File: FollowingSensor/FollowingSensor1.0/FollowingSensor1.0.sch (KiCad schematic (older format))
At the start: 31 parts, among them J1 Conn_01x18, Q1 TEMT7100X01, Q10 TEMT7100X01, Q11 TEMT7100X01, Q12 TEMT7100X01, Q13 TEMT7100X01, Q14 TEMT7100X01, Q2 TEMT7100X01, Q3 TEMT7100X01, Q4 TEMT7100X01, Q5 TEMT7100X01, Q6 TEMT7100X01, Q7 TEMT7100X01, Q8 TEMT7100X01, Q9 TEMT7100X01

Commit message: LinesensorUpdate
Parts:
- D1, D2, D3, D4, D5, D6, D7, D8: symbol Device:LED_ALT -> FollowingSensor1.0-rescue:LED_ALT-Device
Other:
- moved on the sheet: D1, D2, D3, D4, D5, D6, D7, D8, J1, Q1, Q10, Q11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

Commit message: placement phototransister
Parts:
- added D11, D2, D4, D9: SIR19-21C/TR8, Footprint:SIR19-21C, symbol FollowingSensor1.0-rescue:LED_ALT-Device
- added R10, R11, R12, R9: R, Resistor_SMD:R_0603_1608Metric, symbol Device:R
- renumbered D7 to D10, D8 to D12, D2 to D3, D3 to D5, D4 to D6, D5 to D7, D6 to D8, Q14 to Q13, Q13 to Q14
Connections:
- net +3V3: now also R10.1, R11.1, R12.1, R9.1
- net SENSOR_PULSE: now also D11.1 (K), D2.1 (K), D4.1 (K), D9.1 (K)
- new net: D9.2 (A), R10.2
- new net: D11.2 (A), R12.2
- new net: D4.2 (A), R11.2
- new net: D2.2 (A), R9.2
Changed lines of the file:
@@
 $EndComp
 $Comp
-L FollowingSensor1.0-rescue:LED_ALT-Device D5
+L FollowingSensor1.0-rescue:LED_ALT-Device D7
 U 1 1 5F240BF8
 P 8950 2650
-F 0 "D5" V 8989 2532 50  0000 R CNN
+F 0 "D7" V 8989 2532 50  0000 R CNN
 F 1 "SIR19-21C/TR8" V 9100 2600 50  0000 R CNN
 F 2 "Footprint:SIR19-21C" H 8950 2650 50  0001 C CNN
@@
 $EndComp
 $Comp
-L FollowingSensor1.0-rescue:LED_ALT-Device D4
+L FollowingSensor1.0-rescue:LED_ALT-Device D6
 U 1 1 5F2485DD
 P 6950 2600
-F 0 "D4" V 6989 2482 50  0000 R CNN
+F 0 "D6" V 6989 2482 50  0000 R CNN
 F 1 "SIR19-21C/TR8" V 7100 2600 50  0000 R CNN
 F 2 "Footprint:SIR19-21C" H 6950 2600 50  0001 C CNN
@@
 $EndComp
 $Comp
-L FollowingSensor1.0-rescue:LED_ALT-Device D7
+L FollowingSensor1.0-rescue:LED_ALT-Device D10
 U 1 1 5F29282A
 P 11800 7450
-F 0 "D7" V 11839 7332 50  0000 R CNN
+F 0 "D10" V 11839 7332 50  0000 R CNN
 F 1 "SIR19-21C/TR8" V 11950 7400 50  0000 R CNN
 F 2 "Footprint:SIR19-21C" H 11800 7450 50  0001 C CNN
@@
 SENSOR_PULSE
 $Comp
-L Device:Q_Photo_NPN Q14
+L Device:Q_Photo_NPN Q13
 U 1 1 5F292833
 P 12350 7500
-F 0 "Q14" H 12540 7546 50  0000 L CNN
+F 0 "Q13" H 12540 7546 50  0000 L CNN
 F 1 "TEMT7100X01" H 12540 7455 50  0000 L CNN
 F 2 "Footprint:TEMT7100X01" H 12550 7600 50  0001 C CNN
@@
 	12450 6850 12450 7300
 $Comp
-L Device:Q_Photo_NPN Q13
+L Device:Q_Photo_NPN Q14
 U 1 1 5F292858
 P 13850 7450
-F 0 "Q13" H 14040 7496 50  0000 L CNN
+F 0 "Q14" H 14040 7496 50  0000 L CNN
 F 1 "TEMT7100X01" H 14000 7350 50  0000 L CNN
 F 2 "Footprint:TEMT7100X01" H 14050 7550 50  0001 C CNN
@@
 $EndComp
 $Comp
-L FollowingSensor1.0-rescue:LED_ALT-Device D8
+L FollowingSensor1.0-rescue:LED_ALT-Device D12
 U 1 1 5F292874
 P 14500 7450
-F 0 "D8" V 14539 7332 50  0000 R CNN
+F 0 "D12" V 14539 7332 50  0000 R CNN
 F 1 "SIR19-21C/TR8" V 14448 7332 50  0000 R CNN
 F 2 "Footprint:SIR19-21C" H 14500 7450 50  0001 C CNN
@@
 $EndComp
 $Comp
-L FollowingSensor1.0-rescue:LED_ALT-Device D2
+L FollowingSensor1.0-rescue:LED_ALT-Device D3
 U 1 1 5F2A2529
 P 4800 7500
-F 0 "D2" V 4839 7382 50  0000 R CNN
+F 0 "D3" V 4839 7382 50  0000 R CNN
 F 1 "SIR19-21C/TR8" V 4950 7500 50  0000 R CNN
 F 2 "Footprint:SIR19-21C" H 4800 7500 50  0001 C CNN
@@
 	9800 7150 9800 7300
 $Comp
-L FollowingSensor1.0-rescue:LED_ALT-Device D6
+L FollowingSensor1.0-rescue:LED_ALT-Device D8
 U 1 1 5F254403
 P 9800 7450
-F 0 "D6" V 9839 7332 50  0000 R CNN
+F 0 "D8" V 9839 7332 50  0000 R CNN
 F 1 "SIR19-21C/TR8" V 9650 7400 50  0000 R CNN
 F 2 "Footprint:SIR19-21C" H 9800 7450 50  0001 C CNN
@@
 $EndComp
 $Comp
-L FollowingSensor1.0-rescue:LED_ALT-Device D3
+L FollowingSensor1.0-rescue:LED_ALT-Device D5
 U 1 1 5F29F518
 P 7000 7550
-F 0 "D3" V 7039 7432 50  0000 R CNN
+F 0 "D5" V 7039 7432 50  0000 R CNN
 F 1 "SIR19-21C/TR8" V 7200 7550 50  0000 R CNN
 F 2 "Footprint:SIR19-21C" H 7000 7550 50  0001 C CNN
@@
 Wire Wire Line
 	7650 6900 7650 7350
+$Comp
+L power:+3.3V #PWR026
+U 1 1 609A63EE
+P 10800 6700
+F 0 "#PWR026" H 10800 6550 50  0001 C CNN
+F 1 "+3.3V" H 10815 6873 50  0000 C CNN
+F 2 "" H 10800 6700 50  0001 C CNN
+F 3 "" H 10800 6700 50  0001 C CNN
+	1    10800 6700
+	1    0    0    -1
+$EndComp
+Wire Wire Line
+	10800 6700 10800 6850
+$Comp
+L Device:R R10
+U 1 1 609A63F5
+P 10800 7000
+F 0 "R10" H 10870 7046 50  0000 L CNN
+F 1 "R" H 10870 6955 50  0000 L CNN
+F 2 "Resistor_SMD:R_0603_1608Metric" V 10730 7000 50  0001 C CNN
+F 3 "~" H 10800 7000 50  0001 C CNN
+	1    10800 7000
+	1    0    0    -1
+$EndComp
+$Comp
+L FollowingSensor1.0-rescue:LED_ALT-Device D9
+U 1 1 609A63FB
+P 10800 7450
+F 0 "D9" V 10839 7332 50  0000 R CNN
+F 1 "SIR19-21C/TR8" V 10950 7400 50  0000 R CNN
+F 2 "Footprint:SIR19-21C" H 10800 7450 50  0001 C CNN
+F 3 "~" H 10800 7450 50  0001 C CNN
+	1    10800 7450
+	0    -1   -1   0
+$EndComp
+Wire Wire Line
+	10800 7150 10800 7300
+Wire Wire Line
+	10800 7800 10800 7600
+Text GLabel 10800 7800 3    50   Input ~ 0
+SENSOR_PULSE
+$Comp
+L power:+3.3V #PWR028
+U 1 1 609A9208
+P 13200 6750
+F 0 "#PWR028" H 13200 6600 50  0001 C CNN
+F 1 "+3.3V" H 13215 6923 50  0000 C CNN
+F 2 "" H 13200 6750 50  0001 C CNN
+F 3 "" H 13200 6750 50  0001 C CNN
+	1    13200 6750
+	1    0    0    -1
+$EndComp
+Wire Wire Line
+	13200 6750 13200 6900
+$Comp
+L Device:R R12
+U 1 1 609A920F
+P 13200 7050
+F 0 "R12" H 13270 7096 50  0000 L CNN
+F 1 "R" H 13270 7005 50  0000 L CNN
+F 2 "Resistor_SMD:R_0603_1608Metric" V 13130 7050 50  0001 C CNN
+F 3 "~" H 13200 7050 50  0001 C CNN
+	1    13200 7050
+	1    0    0    -1
+$EndComp
+$Comp
+L FollowingSensor1.0-rescue:LED_ALT-Device D11
+U 1 1 609A9215
+P 13200 7500
+F 0 "D11" V 13239 7382 50  0000 R CNN
+F 1 "SIR19-21C/TR8" V 13350 7450 50  0000 R CNN
+F 2 "Footprint:SIR19-21C" H 13200 7500 50  0001 C CNN
+F 3 "~" H 13200 7500 50  0001 C CNN
+	1    13200 7500
+	0    -1   -1   0
+$EndComp
+Wire Wire Line
+	13200 7200 13200 7350
+Wire Wire Line
+	13200 7850 13200 7650
+Text GLabel 13200 7850 3    50   Input ~ 0
+SENSOR_PULSE
+$Comp
+L power:+3.3V #PWR027
+U 1 1 609AC454
+P 5900 6750
+F 0 "#PWR027" H 5900 6600 50  0001 C CNN
+F 1 "+3.3V" H 5915 6923 50  0000 C CNN
+F 2 "" H 5900 6750 50  0001 C CNN
+F 3 "" H 5900 6750 50  0001 C CNN
+	1    5900 6750
+	1    0    0    -1
+$EndComp
+Wire Wire Line
+	5900 6750 5900 6900
+$Comp
+L Device:R R11
+U 1 1 609AC45B
+P 5900 7050
+F 0 "R11" H 5970 7096 50  0000 L CNN
+F 1 "R" H 5970 7005 50  0000 L CNN
+F 2 "Resistor_SMD:R_0603_1608Metric" V 5830 7050 50  0001 C CNN
+F 3 "~" H 5900 7050 50  0001 C CNN
+	1    5900 7050
+	1    0    0    -1
+$EndComp
+$Comp
+L FollowingSensor1.0-rescue:LED_ALT-Device D4
+U 1 1 609AC461
+P 5900 7500
+F 0 "D4" V 5939 7382 50  0000 R CNN
+F 1 "SIR19-21C/TR8" V 6050 7450 50  0000 R CNN
+F 2 "Footprint:SIR19-21C" H 5900 7500 50  0001 C CNN
+F 3 "~" H 5900 7500 50  0001 C CNN
+	1    5900 7500
+	0    -1   -1   0
+$EndComp
+Wire Wire Line
+	5900 7200 5900 7350
+Wire Wire Line
+	5900 7850 5900 7650
+Text GLabel 5900 7850 3    50   Input ~ 0
+SENSOR_PULSE
+$Comp
+L power:+3.3V #PWR025
+U 1 1 609AF46E
+P 3850 6700
+F 0 "#PWR025" H 3850 6550 50  0001 C CNN
+F 1 "+3.3V" H 3865 6873 50  0000 C CNN
+F 2 "" H 3850 6700 50  0001 C CNN
+F 3 "" H 3850 6700 50  0001 C CNN
+	1    3850 6700
+	1    0    0    -1
+$EndComp
+Wire Wire Line
+	3850 6700 3850 6850
+$Comp
+L Device:R R9
+U 1 1 609AF475
+P 3850 7000
+F 0 "R9" H 3920 7046 50  0000 L CNN
+F 1 "R" H 3920 6955 50  0000 L CNN
+F 2 "Resistor_SMD:R_0603_1608Metric" V 3780 7000 50  0001 C CNN
+F 3 "~" H 3850 7000 50  0001 C CNN
+	1    3850 7000
+	1    0    0    -1
+$EndComp
+$Comp
+L FollowingSensor1.0-rescue:LED_ALT-Device D2
+U 1 1 609AF47B
+P 3850 7450
+F 0 "D2" V 3889 7332 50  0000 R CNN
+F 1 "SIR19-21C/TR8" V 4000 7400 50  0000 R CNN
+F 2 "Footprint:SIR19-21C" H 3850 7450 50  0001 C CNN
+F 3 "~" H 3850 7450 50  0001 C CNN
+	1    3850 7450
+	0    -1   -1   0
+$EndComp
+Wire Wire Line
+	3850 7150 3850 7300
+Wire Wire Line
+	3850 7800 3850 7600
+Text GLabel 3850 7800 3    50   Input ~ 0
+SENSOR_PULSE
 $EndSCHEMATC

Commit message: following sensor designed
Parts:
- added C1: 1u, Capacitor_SMD:C_0603_1608Metric, symbol Device:C_Small
- renumbered R7 to R10, R12 to R11, R8 to R12, R9 to R2, R2 to R3, R11 to R4, R3 to R5, R4 to R6, R5 to R7, R6 to R8, R10 to R9
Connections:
- net +3V3: now also J1.18 (Pin_18), C1.1; no longer J1.1 (Pin_1)
- net AD1: now also J1.17 (Pin_17); no longer J1.2 (Pin_2)
- net AD10: now also J1.8 (Pin_8); no longer J1.11 (Pin_11)
- net AD11: now also J1.7 (Pin_7); no longer J1.12 (Pin_12)
- net AD12: now also J1.6 (Pin_6); no longer J1.13 (Pin_13)
- net AD13: now also J1.5 (Pin_5); no longer J1.14 (Pin_14)
- net AD14: now also J1.4 (Pin_4); no longer J1.15 (Pin_15)
- net AD2: now also J1.16 (Pin_16); no longer J1.3 (Pin_3)
- net AD3: now also J1.15 (Pin_15); no longer J1.4 (Pin_4)
- net AD4: now also J1.14 (Pin_14); no longer J1.5 (Pin_5)
- net AD5: now also J1.13 (Pin_13); no longer J1.6 (Pin_6)
- net AD6: now also J1.12 (Pin_12); no longer J1.7 (Pin_7)
- net AD7: now also J1.11 (Pin_11); no longer J1.8 (Pin_8)
- net AD8: now also J1.10 (Pin_10); no longer J1.9 (Pin_9)
- net AD9: now also J1.9 (Pin_9); no longer J1.10 (Pin_10)
- net GND: now also J1.1 (Pin_1), C1.2; no longer J1.18 (Pin_18)
- net SENSOR_PULSE: now also J1.3 (Pin_3); no longer J1.16 (Pin_16)
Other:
- moved on the sheet: D10, D11, D12, D8, D9, Q10, Q11, Q12, Q13, Q14, R10, R11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

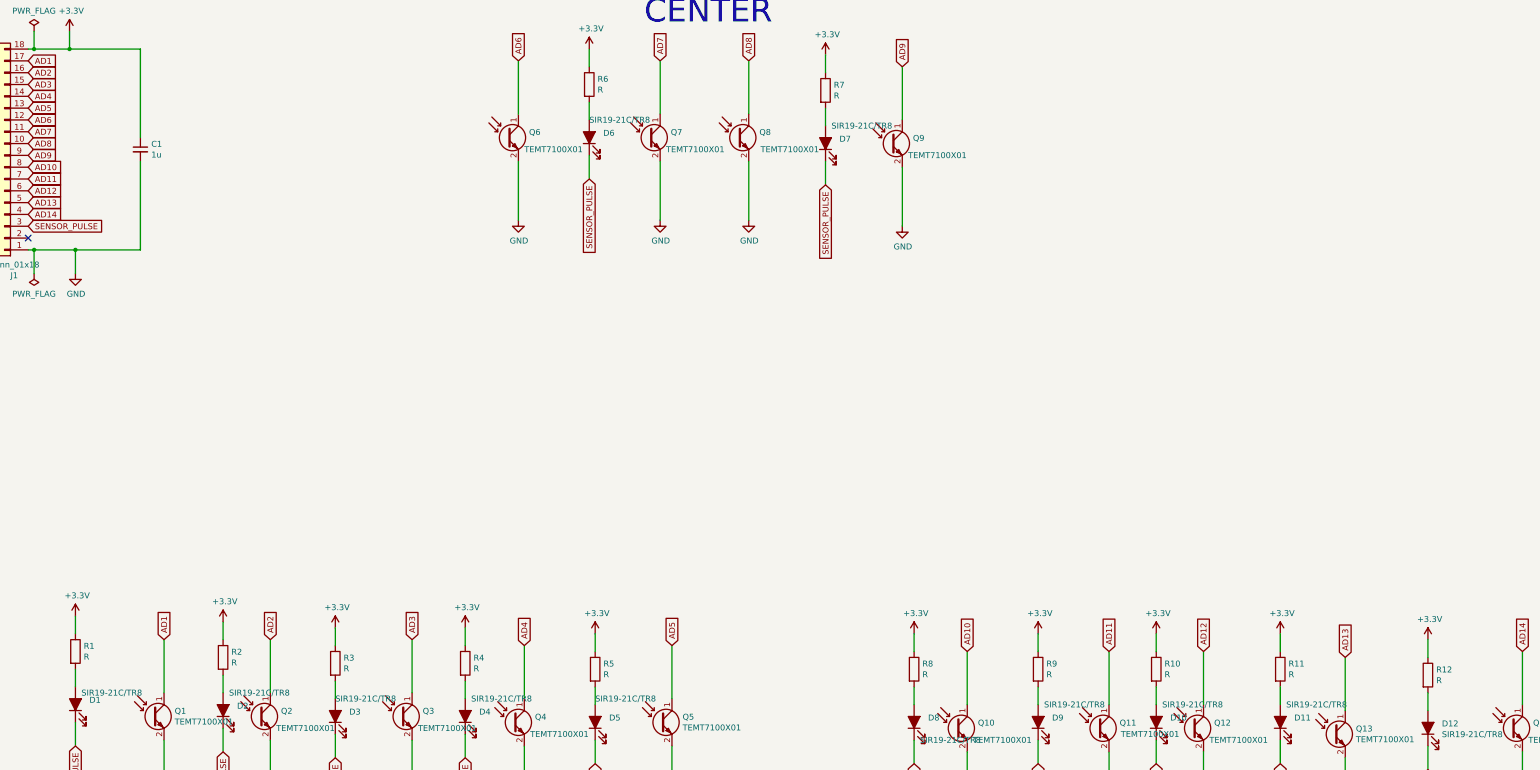
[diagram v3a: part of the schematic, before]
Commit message: センサの抵抗値などを変更
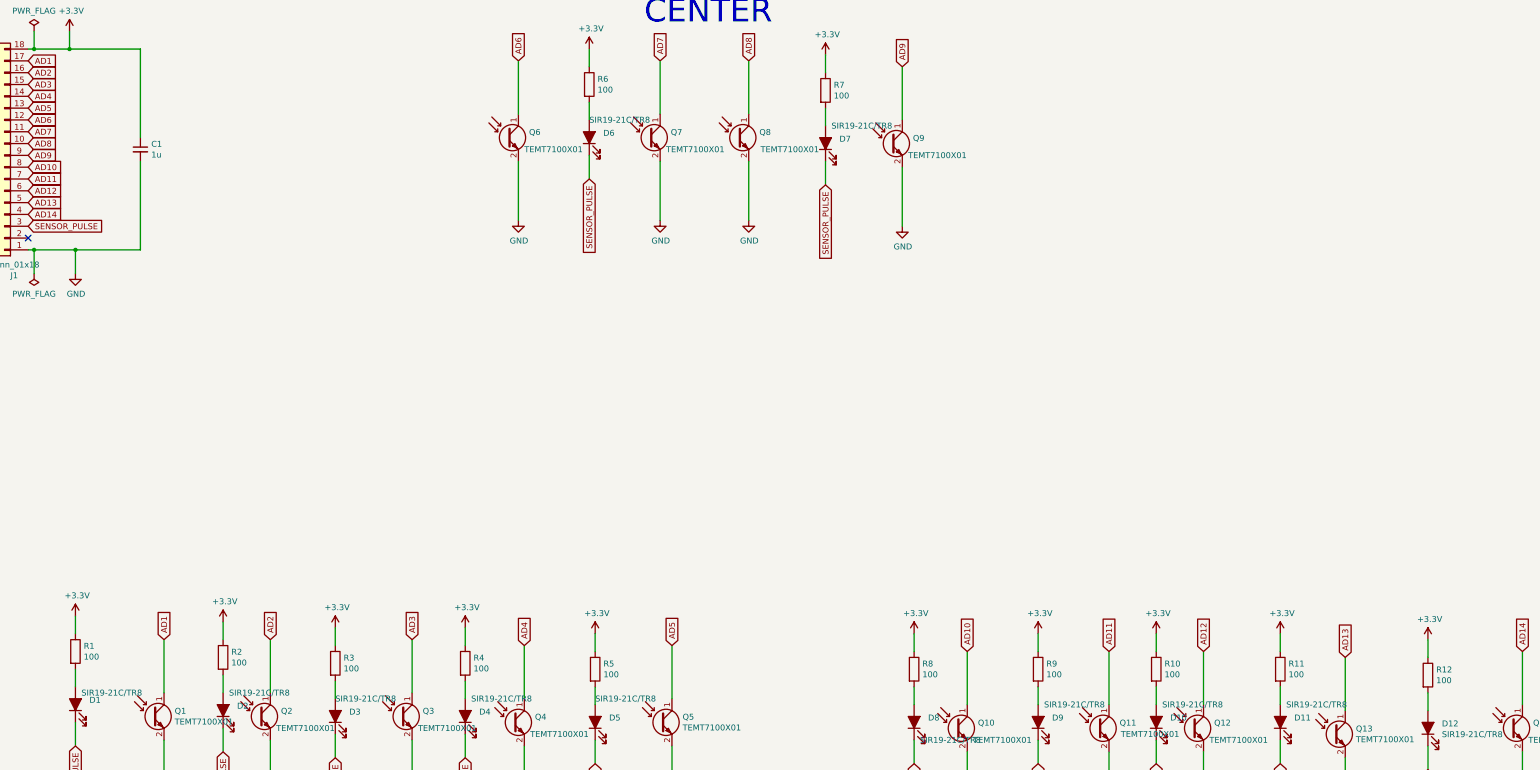
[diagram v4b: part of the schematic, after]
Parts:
- R1, R10, R11, R12, R2, R3, R4, R5, R6, R7, R8, R9: value R -> 100
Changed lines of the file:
@@
 P 8950 2200
 F 0 "R7" H 9020 2246 50  0000 L CNN
-F 1 "R" H 9020 2155 50  0000 L CNN
+F 1 "100" H 9020 2155 50  0000 L CNN
 F 2 "Resistor_SMD:R_0603_1608Metric" V 8880 2200 50  0001 C CNN
 F 3 "~" H 8950 2200 50  0001 C CNN
@@
 P 6950 2150
 F 0 "R6" H 7020 2196 50  0000 L CNN
-F 1 "R" H 7020 2105 50  0000 L CNN
+F 1 "100" H 7020 2105 50  0000 L CNN
 F 2 "Resistor_SMD:R_0603_1608Metric" V 6880 2150 50  0001 C CNN
 F 3 "~" H 6950 2150 50  0001 C CNN
@@
 P 4800 7050
 F 0 "R3" H 4870 7096 50  0000 L CNN
-F 1 "R" H 4870 7005 50  0000 L CNN
+F 1 "100" H 4870 7005 50  0000 L CNN
 F 2 "Resistor_SMD:R_0603_1608Metric" V 4730 7050 50  0001 C CNN
 F 3 "~" H 4800 7050 50  0001 C CNN
@@
 P 2600 6950
 F 0 "R1" H 2670 6996 50  0000 L CNN
-F 1 "R" H 2670 6905 50  0000 L CNN
+F 1 "100" H 2670 6905 50  0000 L CNN
 F 2 "Resistor_SMD:R_0603_1608Metric" V 2530 6950 50  0001 C CNN
 F 3 "~" H 2600 6950 50  0001 C CNN
@@
 P 7000 7100
 F 0 "R5" H 7070 7146 50  0000 L CNN
-F 1 "R" H 7070 7055 50  0000 L CNN
+F 1 "100" H 7070 7055 50  0000 L CNN
 F 2 "Resistor_SMD:R_0603_1608Metric" V 6930 7100 50  0001 C CNN
 F 3 "~" H 7000 7100 50  0001 C CNN
@@
 P 5900 7050
 F 0 "R4" H 5970 7096 50  0000 L CNN
-F 1 "R" H 5970 7005 50  0000 L CNN
+F 1 "100" H 5970 7005 50  0000 L CNN
 F 2 "Resistor_SMD:R_0603_1608Metric" V 5830 7050 50  0001 C CNN
 F 3 "~" H 5900 7050 50  0001 C CNN
@@
 P 3850 7000
 F 0 "R2" H 3920 7046 50  0000 L CNN
-F 1 "R" H 3920 6955 50  0000 L CNN
+F 1 "100" H 3920 6955 50  0000 L CNN
 F 2 "Resistor_SMD:R_0603_1608Metric" V 3780 7000 50  0001 C CNN
 F 3 "~" H 3850 7000 50  0001 C CNN
@@
 P 11750 7100
 F 0 "R10" H 11820 7146 50  0000 L CNN
-F 1 "R" H 11820 7055 50  0000 L CNN
+F 1 "100" H 11820 7055 50  0000 L CNN
 F 2 "Resistor_SMD:R_0603_1608Metric" V 11680 7100 50  0001 C CNN
 F 3 "~" H 11750 7100 50  0001 C CNN
@@
 P 14050 7150
 F 0 "R12" H 14120 7196 50  0000 L CNN
-F 1 "R" H 14120 7105 50  0000 L CNN
+F 1 "100" H 14120 7105 50  0000 L CNN
 F 2 "Resistor_SMD:R_0603_1608Metric" V 13980 7150 50  0001 C CNN
 F 3 "~" H 14050 7150 50  0001 C CNN
@@
 P 9700 7100
 F 0 "R8" H 9770 7146 50  0000 L CNN
-F 1 "R" H 9770 7055 50  0000 L CNN
+F 1 "100" H 9770 7055 50  0000 L CNN
 F 2 "Resistor_SMD:R_0603_1608Metric" V 9630 7100 50  0001 C CNN
 F 3 "~" H 9700 7100 50  0001 C CNN
@@
 P 10750 7100
 F 0 "R9" H 10820 7146 50  0000 L CNN
-F 1 "R" H 10820 7055 50  0000 L CNN
+F 1 "100" H 10820 7055 50  0000 L CNN
 F 2 "Resistor_SMD:R_0603_1608Metric" V 10680 7100 50  0001 C CNN
 F 3 "~" H 10750 7100 50  0001 C CNN
@@
 P 12800 7100
 F 0 "R11" H 12870 7146 50  0000 L CNN
-F 1 "R" H 12870 7055 50  0000 L CNN
+F 1 "100" H 12870 7055 50  0000 L CNN
 F 2 "Resistor_SMD:R_0603_1608Metric" V 12730 7100 50  0001 C CNN
 F 3 "~" H 12800 7100 50  0001 C CNN
